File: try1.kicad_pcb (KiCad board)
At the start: 2 copper layers, 175.3 x 119.4 mm, 33 parts, among them J10 Archon-connector-modules-Driv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, J11 Archon-connector-modules-Driv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, J2 Archon-connector-modules-Heat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, J21 DB37, J22 DB37, J3 Archon-connector-modules-Driv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, J31 DB9, J4 Archon-connector-modules-LVBi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, J41 CONN_DVI, J5 Archon-connector-modules-ADC, J6 Archon-connector-modules-ADC, J7 Archon-connector-modules-ADC, J8 Archon-connector-modules-ADC, J9 Archon-connector-modules-HVBi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, P1 CONN_02X02

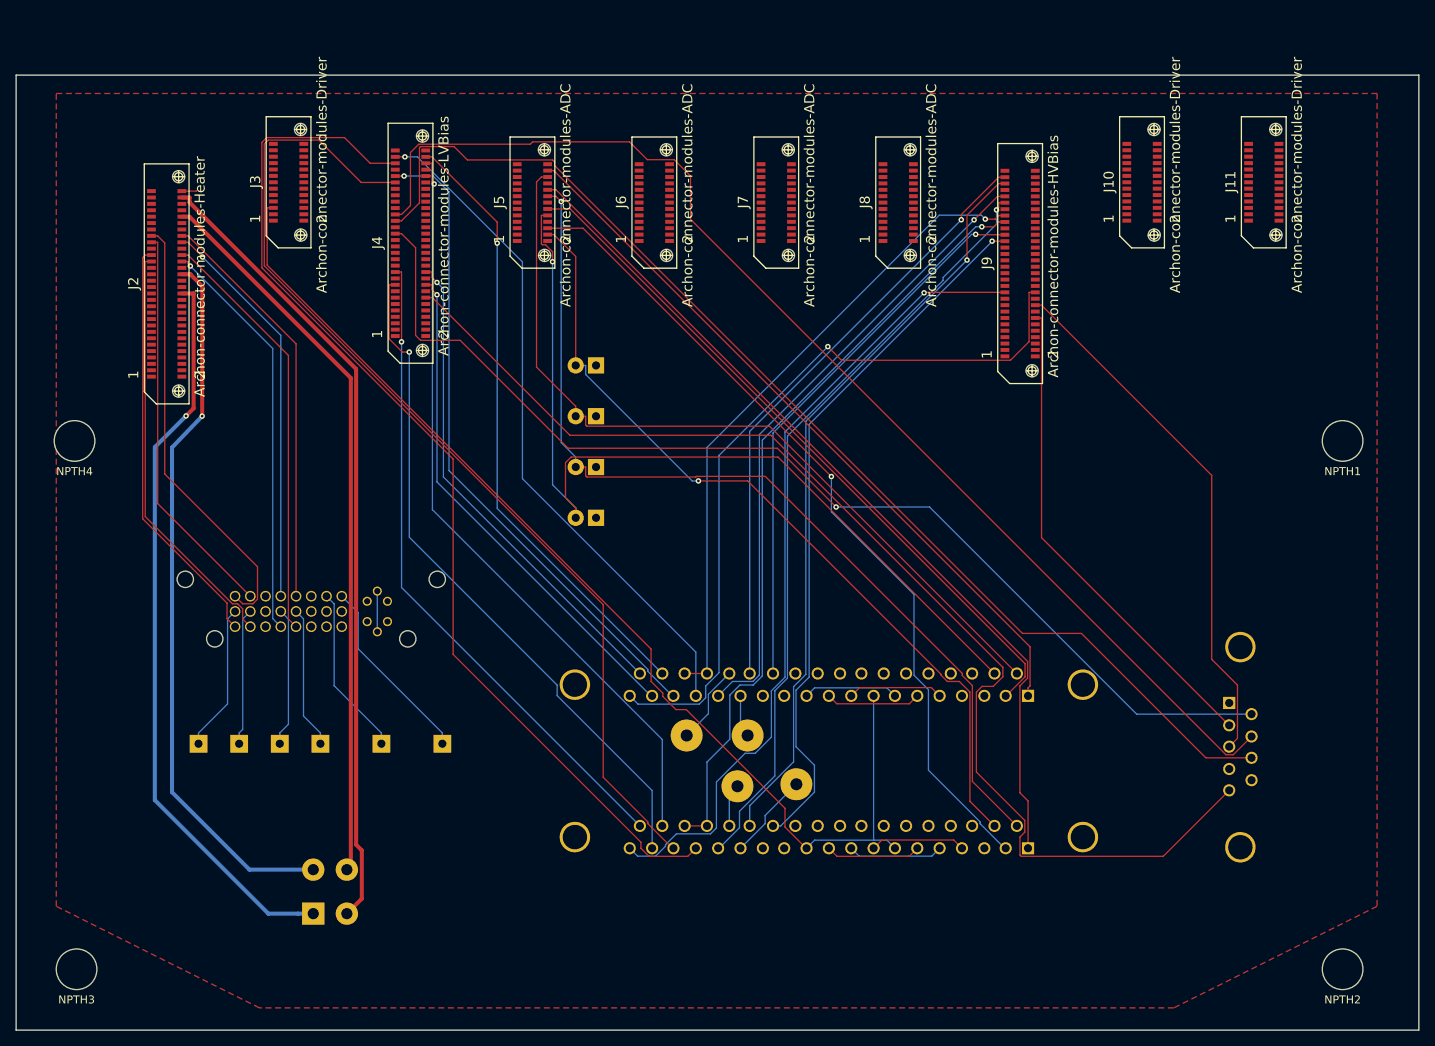
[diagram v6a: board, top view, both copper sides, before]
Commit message: Delete More Old Traces
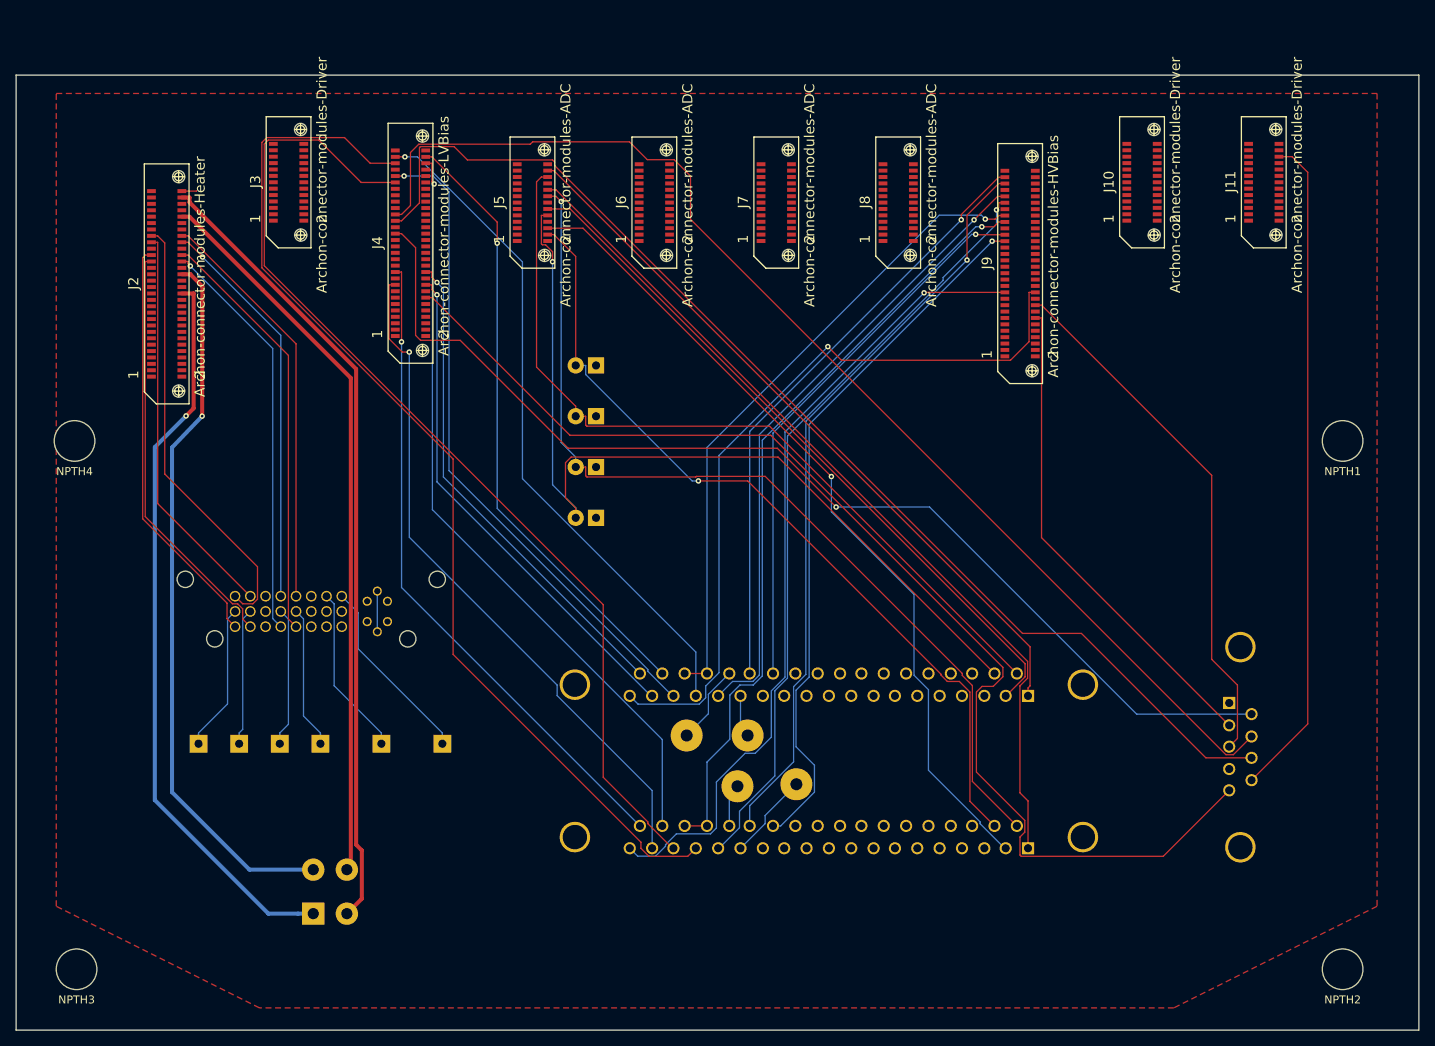
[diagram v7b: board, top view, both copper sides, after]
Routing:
- net DRV3_CH6: track 110.2 -> 0.05 mm
- net DRV11_CH1: track 0.00 -> 83.3 mm
- net DRV10_CH4: track 27.0 -> 0.00 mm
- net DRV3_CH8: track 11.2 -> 0.00 mm
- net DRV10_CH3: track 10.5 -> 0.00 mm
- net DRV10_CH5: track 10.5 -> 0.00 mm
- net DRV10_CH7: track 10.5 -> 0.00 mm
- net DRV10_CH1: track 10.4 -> 0.00 mm
- net DRV10_CH2: track 10.4 -> 0.00 mm
- net DRV11_CH2: track 1.46 -> 0.00 mm
- net DRV3_CH1: track 1.53 -> 0.08 mm
- net DRV10_CH6: track 1.44 -> 0.00 mm
- net DRV3_CH7: track 1.50 -> 0.08 mm
- net DRV10_CH8: track 1.42 -> 0.00 mm
- net DRV3_CH5: track 1.48 -> 0.08 mm
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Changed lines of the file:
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@@
   (general
     (links 128)
-    (no_connects 54)
+    (no_connects 53)
     (area 45.767299 23.087299 221.132701 142.492701)
     (thickness 1.6)
     (drawings 7)
-    (tracks 518)
+    (tracks 488)
     (zones 0)
     (modules 33)
@@
   (segment (start 66.4999 38.4025) (end 67.4565 38.4025) (width 0.508) (layer F.Cu) (net 57))
   (segment (start 147.302 119.747) (end 147.38 119.747) (width 0.1524) (layer F.Cu) (net 59))
-  (segment (start 147.38 119.747) (end 148.388 120.756) (width 0.1524) (layer F.Cu) (net 59))
-  (segment (start 145.588 99.6951) (end 144.586 100.697) (width 0.1524) (layer B.Cu) (net 60))
-  (segment (start 154.633 99.6951) (end 145.588 99.6951) (width 0.1524) (layer B.Cu) (net 60))
-  (segment (start 77.9401 39.6979) (end 77.1613 39.6979) (width 0.1524) (layer F.Cu) (net 60))
-  (segment (start 147.38 100.697) (end 148.373 101.69) (width 0.1524) (layer F.Cu) (net 65))
   (segment (start 147.302 100.697) (end 147.38 100.697) (width 0.1524) (layer F.Cu) (net 65))
   (segment (start 144.539 119.747) (end 144.586 119.747) (width 0.1524) (layer F.Cu) (net 66))
-  (segment (start 141.889 117.096) (end 144.539 119.747) (width 0.1524) (layer F.Cu) (net 66))
-  (segment (start 141.889 114.746) (end 141.889 117.096) (width 0.1524) (layer F.Cu) (net 66))
-  (segment (start 129.557 102.415) (end 141.889 114.746) (width 0.1524) (layer F.Cu) (net 66))
-  (segment (start 128.259 102.415) (end 129.557 102.415) (width 0.1524) (layer F.Cu) (net 66))
-  (segment (start 126.616 100.771) (end 128.259 102.415) (width 0.1524) (layer F.Cu) (net 66))
-  (segment (start 126.616 100.355) (end 126.616 100.771) (width 0.1524) (layer F.Cu) (net 66))
-  (segment (start 125.155 98.894) (end 126.616 100.355) (width 0.1524) (layer F.Cu) (net 66))
-  (segment (start 125.155 94.8511) (end 125.155 98.894) (width 0.1524) (layer F.Cu) (net 66))
-  (segment (start 77.1613 46.8574) (end 125.155 94.8511) (width 0.1524) (layer F.Cu) (net 66))
-  (segment (start 77.1613 39.6979) (end 77.1613 46.8574) (width 0.1524) (layer F.Cu) (net 66))
-  (segment (start 144.586 119.747) (end 145.603 118.73) (width 0.1524) (layer B.Cu) (net 66))
   (segment (start 150.096 119.747) (end 150.174 119.747) (width 0.1524) (layer F.Cu) (net 71))
-  (segment (start 150.174 119.747) (end 151.166 120.739) (width 0.1524) (layer B.Cu) (net 71))
   (segment (start 150.096 100.697) (end 150.174 100.697) (width 0.1524) (layer F.Cu) (net 77))
-  (segment (start 150.174 100.697) (end 151.204 99.6673) (width 0.1524) (layer F.Cu) (net 77))
   (segment (start 97.81 50.9196) (end 96.9799 50.9196) (width 0.1524) (layer F.Cu) (net 91))
   (segment (start 115.015 68.1246) (end 97.81 50.9196) (width 0.1524) (layer F.Cu) (net 91))
@@
   (segment (start 169.38 35.8625) (end 168.601 35.8625) (width 0.1524) (layer F.Cu) (net 288))
   (segment (start 169.38 35.8625) (end 169.3801 35.8625) (width 0.1524) (layer F.Cu) (net 288))
-  (segment (start 155.635 100.697) (end 154.633 99.6951) (width 0.1524) (layer B.Cu) (net 293))
-  (segment (start 160.193 99.6673) (end 161.223 100.697) (width 0.1524) (layer F.Cu) (net 303))
-  (segment (start 151.204 99.6673) (end 160.193 99.6673) (width 0.1524) (layer F.Cu) (net 303))
   (segment (start 188.42 33.3021) (end 188.4199 33.3021) (width 0.1524) (layer F.Cu) (net 303))
-  (segment (start 152.968 119.747) (end 153.999 118.716) (width 0.1524) (layer F.Cu) (net 304))
-  (segment (start 153.999 118.716) (end 162.986 118.716) (width 0.1524) (layer F.Cu) (net 304))
   (segment (start 184.62 32.502) (end 184.6201 32.502) (width 0.1524) (layer F.Cu) (net 304))
   (segment (start 139.404 116.674) (end 136.331 119.747) (width 0.1524) (layer B.Cu) (net 321))
@@
   (segment (start 99.06 105.334) (end 88.5397 94.8132) (width 0.1524) (layer B.Cu) (net 355))
   (segment (start 99.06 106.68) (end 99.06 105.334) (width 0.1524) (layer B.Cu) (net 355))
-  (segment (start 157.42 120.756) (end 158.429 119.747) (width 0.1524) (layer F.Cu) (net 356))
-  (segment (start 148.388 120.756) (end 157.42 120.756) (width 0.1524) (layer F.Cu) (net 356))
   (segment (start 188.42 38.8978) (end 188.4199 38.8978) (width 0.1524) (layer F.Cu) (net 357))
-  (segment (start 157.436 101.69) (end 158.429 100.697) (width 0.1524) (layer F.Cu) (net 358))
-  (segment (start 148.373 101.69) (end 157.436 101.69) (width 0.1524) (layer F.Cu) (net 358))
-  (segment (start 154.618 118.73) (end 155.635 119.747) (width 0.1524) (layer B.Cu) (net 359))
-  (segment (start 160.231 120.739) (end 161.223 119.747) (width 0.1524) (layer B.Cu) (net 360))
-  (segment (start 151.166 120.739) (end 160.231 120.739) (width 0.1524) (layer B.Cu) (net 360))
-  (segment (start 152.968 100.697) (end 152.968 118.73) (width 0.1524) (layer B.Cu) (net 361))
-  (segment (start 145.603 118.73) (end 152.968 118.73) (width 0.1524) (layer B.Cu) (net 361))
-  (segment (start 152.968 118.73) (end 154.618 118.73) (width 0.1524) (layer B.Cu) (net 361))
-  (segment (start 162.986 118.716) (end 164.017 119.747) (width 0.1524) (layer F.Cu) (net 369))
+  (segment (start 203.63992 33.30214) (end 205.28554 33.30214) (width 0.1524) (layer F.Cu) (net 368))
+  (segment (start 207.2386 104.2114) (end 200.212 111.238) (width 0.1524) (layer F.Cu) (net 368))
+  (segment (start 207.2386 35.2552) (end 207.2386 104.2114) (width 0.1524) (layer F.Cu) (net 368))
+  (segment (start 205.28554 33.30214) (end 207.2386 35.2552) (width 0.1524) (layer F.Cu) (net 368))
   (zone (net 23) (net_name /GND) (layer F.Cu) (hatch edge 0.508)
     (connect_pads (clearance 0.508))

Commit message: After FreeRoute Of Only New DRV Connections
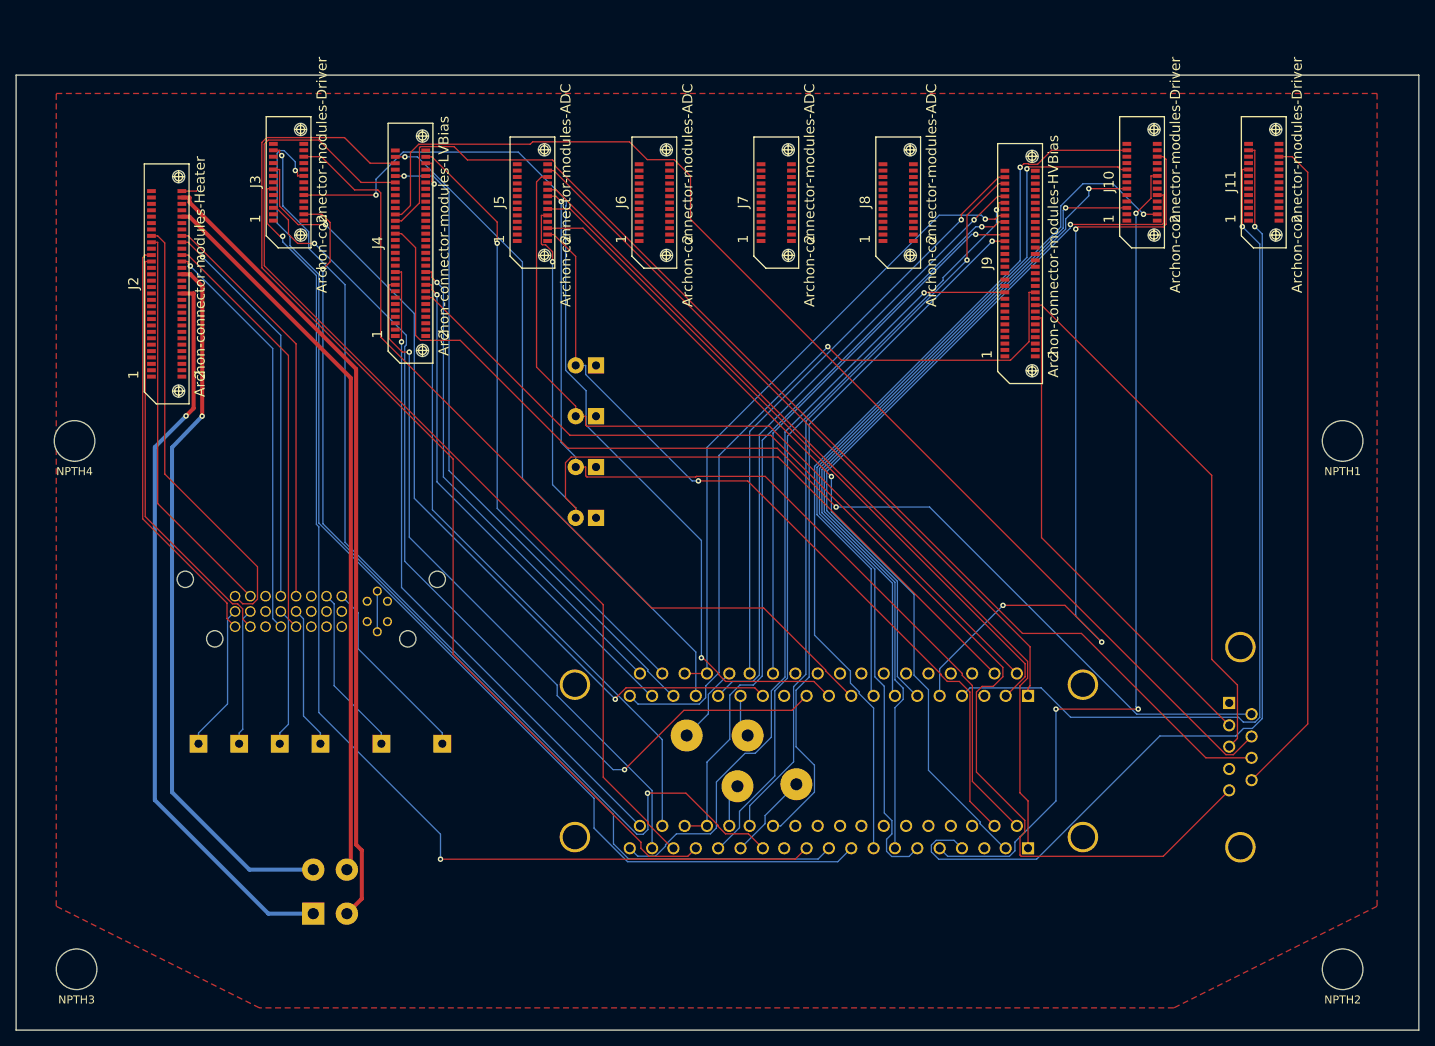
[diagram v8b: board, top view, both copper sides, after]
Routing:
- net DRV3_CH3: track 0.08 -> 141.1 mm, vias 0 -> 1
- net DRV3_CH6: track 0.05 -> 140.1 mm, vias 0 -> 2
- net DRV3_CH2: track 0.00 -> 128.3 mm, vias 0 -> 2
- net DRV11_CH2: track 0.00 -> 126.6 mm, vias 0 -> 1
- net DRV3_CH7: track 0.08 -> 125.2 mm, vias 0 -> 1
- net DRV3_CH5: track 0.08 -> 120.9 mm, vias 0 -> 2
- net DRV3_CH8: track 0.00 -> 117.4 mm, vias 0 -> 2
- net DRV10_CH7: track 0.00 -> 116.5 mm, vias 0 -> 1
- net DRV10_CH2: track 0.00 -> 113.1 mm, vias 0 -> 1
- net DRV11_CH4: track 0.00 -> 109.8 mm, vias 0 -> 1
- net DRV10_CH3: track 0.00 -> 108.6 mm, vias 0 -> 3
- net DRV3_CH1: track 0.08 -> 107.0 mm
- net DRV3_CH4: track 0.00 -> 105.9 mm, vias 0 -> 2
- net DRV10_CH6: track 0.00 -> 105.4 mm, vias 0 -> 1
- net DRV10_CH1: track 0.00 -> 102.7 mm, vias 0 -> 3
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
